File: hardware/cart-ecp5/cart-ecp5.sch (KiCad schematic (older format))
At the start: 10 parts, among them U3 FAN53541

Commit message: Remove superfluous DC-DC converter
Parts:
- removed C1: 10u, Capacitor_SMD:C_0603_1608Metric, symbol Device:C
- removed C2: 10n, Capacitor_SMD:C_0402_1005Metric, symbol Device:C
- removed C3, C4: 10u, Capacitor_SMD:C_0402_1005Metric, symbol Device:C
- removed L1: 470n, Inductor_SMD:L_0805_2012Metric, symbol Device:L
- removed R2, R3, R4: 100k, Resistor_SMD:R_0402_1005Metric, symbol Device:R
- removed R5: 267k, Resistor_SMD:R_0402_1005Metric, symbol Device:R
- removed U3: FAN53541, Package_CSP:WLCSP-20_1.934x2.434mm_Layout4x5_P0.4mm, symbol ng_pmic:FAN53541
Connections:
- net labels removed: FB1V1, GND, P1V1, P3V3, PGOOD_1V1, SW1V1
- wire segments 68 -> 0

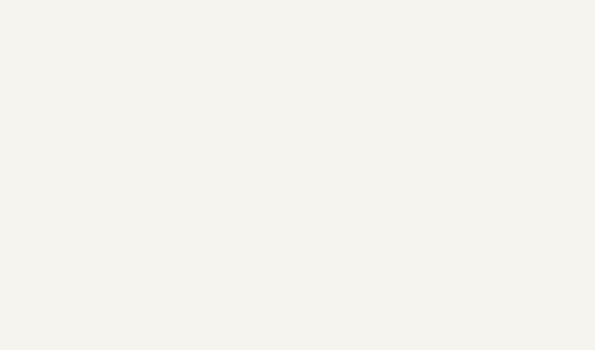
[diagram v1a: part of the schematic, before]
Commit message: Add length matching verifier script
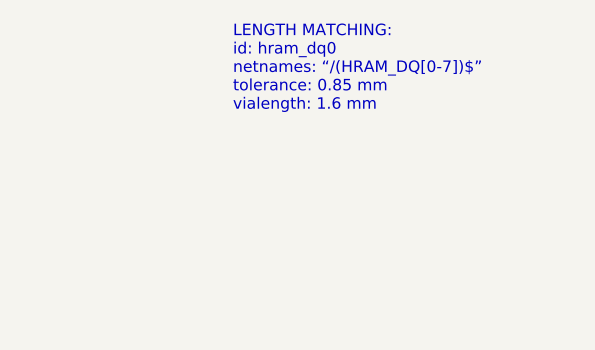
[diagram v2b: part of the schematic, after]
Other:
- note added: "LENGTH MATCHING:\nid: hram_dq0\nnetnames: “/(HRAM_DQ[0-7])$”\ntolerance: 0.85 mm\nvialength: 1.6 mm"
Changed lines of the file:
@@
 F1 "Interface-USB.sch" 50
 $EndSheet
+Text Notes 16850 1200 0    50   ~ 0
+LENGTH MATCHING:\nid: hram_dq0\nnetnames: “/(HRAM_DQ[0-7])$”\ntolerance: 0.85 mm\nvialength: 1.6 mm
 $EndSCHEMATC

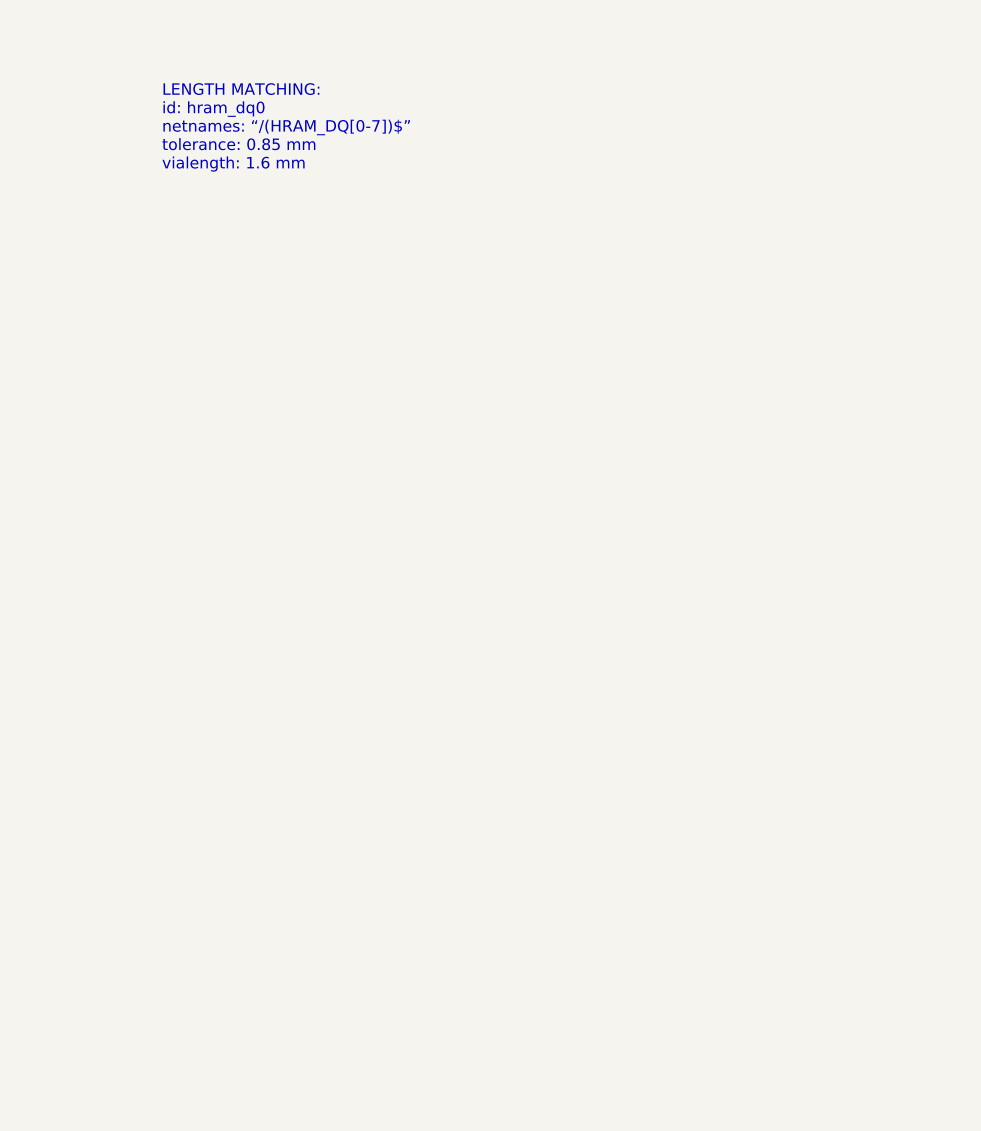
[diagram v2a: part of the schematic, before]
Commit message: Fixes to length matching script, now configured for hyperram
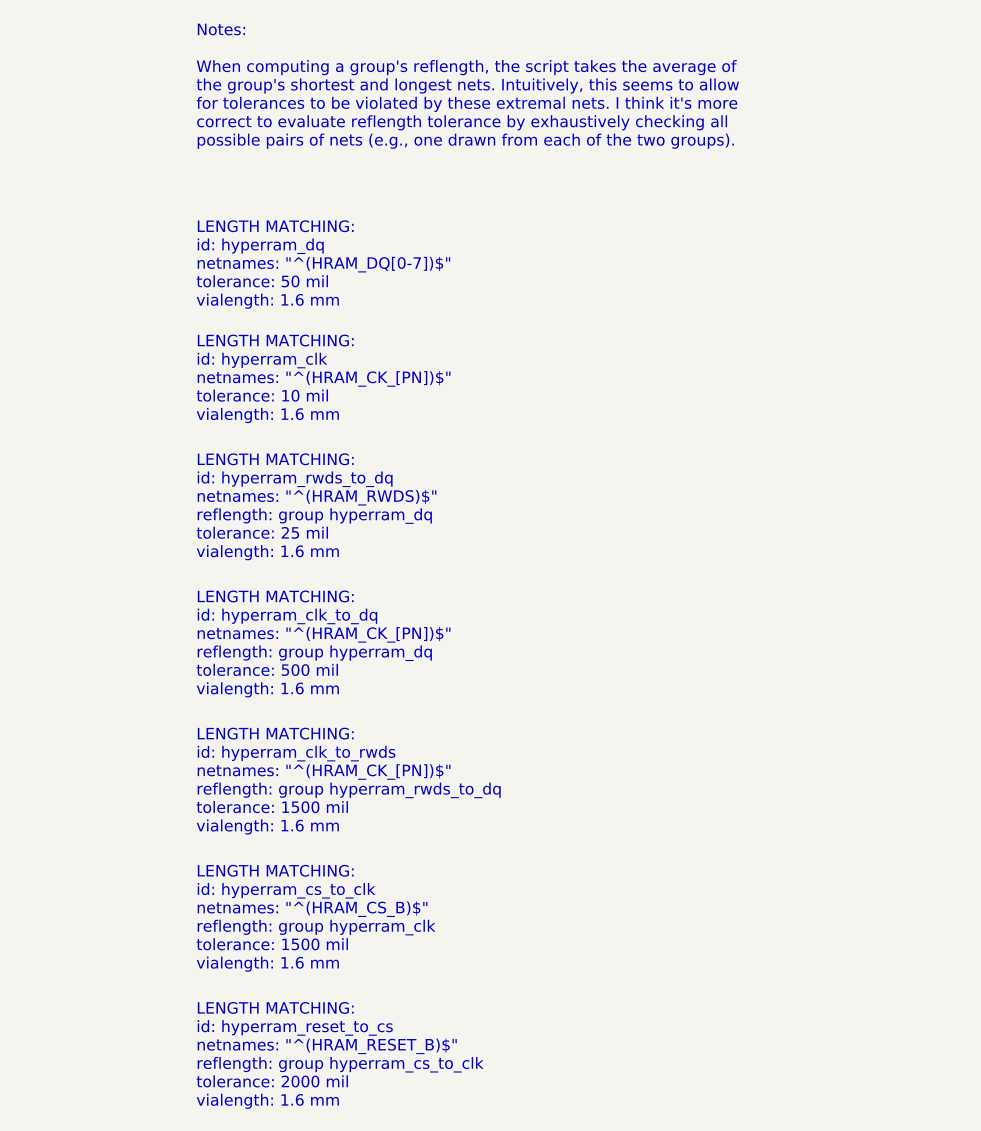
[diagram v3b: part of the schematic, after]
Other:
- note added: "LENGTH MATCHING:\nid: hyperram_clk\nnetnames: "^(HRAM_CK_[PN])$"\ntolerance: 10 mil\nvialength: 1.6 mm"
- note added: "LENGTH MATCHING:\nid: hyperram_clk_to_dq\nnetnames: "^(HRAM_CK_[PN])$"\nreflength: group hyperram_dq\ntolerance: 500 mil\nvialength: 1.6 mm"
- note added: "LENGTH MATCHING:\nid: hyperram_clk_to_rwds\nnetnames: "^(HRAM_CK_[PN])$"\nreflength: group hyperram_rwds_to_dq\ntolerance: 1500 mil\nvialength: 1.6 mm"
- note added: "LENGTH MATCHING:\nid: hyperram_cs_to_clk\nnetnames: "^(HRAM_CS_B)$"\nreflength: group hyperram_clk\ntolerance: 1500 mil\nvialength: 1.6 mm"
- note added: "LENGTH MATCHING:\nid: hyperram_dq\nnetnames: "^(HRAM_DQ[0-7])$"\ntolerance: 50 mil\nvialength: 1.6 mm"
- note added: "LENGTH MATCHING:\nid: hyperram_reset_to_cs\nnetnames: "^(HRAM_RESET_B)$"\nreflength: group hyperram_cs_to_clk\ntolerance: 2000 mil\nvialength: 1.6 mm"
- note added: "LENGTH MATCHING:\nid: hyperram_rwds_to_dq\nnetnames: "^(HRAM_RWDS)$"\nreflength: group hyperram_dq\ntolerance: 25 mil\nvialength: 1.6 mm"
- note added: "Notes:\n\nWhen computing a group's reflength, the script takes the average of\nthe group's shortest and longest nets. Intuitively, this seems to allow\nfor tolerances to be violated by these extremal nets. I think it's more\ncorrect to evaluate reflength tolerance by exhaustively checking all\npossible pairs of nets (e.g., one drawn from each of the two groups)."
- note removed: "LENGTH MATCHING:\nid: hram_dq0\nnetnames: “/(HRAM_DQ[0-7])$”\ntolerance: 0.85 mm\nvialength: 1.6 mm"
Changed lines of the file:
@@
 F1 "Interface-USB.sch" 50
 $EndSheet
-Text Notes 16850 1200 0    50   ~ 0
-LENGTH MATCHING:\nid: hram_dq0\nnetnames: “/(HRAM_DQ[0-7])$”\ntolerance: 0.85 mm\nvialength: 1.6 mm
+Text Notes 17000 1800 0    50   ~ 0
+LENGTH MATCHING:\nid: hyperram_dq\nnetnames: "^(HRAM_DQ[0-7])$"\ntolerance: 50 mil\nvialength: 1.6 mm
+Text Notes 17000 2900 0    50   ~ 0
+LENGTH MATCHING:\nid: hyperram_rwds_to_dq\nnetnames: "^(HRAM_RWDS)$"\nreflength: group hyperram_dq\ntolerance: 25 mil\nvialength: 1.6 mm
+Text Notes 17000 2300 0    50   ~ 0
+LENGTH MATCHING:\nid: hyperram_clk\nnetnames: "^(HRAM_CK_[PN])$"\ntolerance: 10 mil\nvialength: 1.6 mm
+Text Notes 17000 3500 0    50   ~ 0
+LENGTH MATCHING:\nid: hyperram_clk_to_dq\nnetnames: "^(HRAM_CK_[PN])$"\nreflength: group hyperram_dq\ntolerance: 500 mil\nvialength: 1.6 mm
+Text Notes 17000 4100 0    50   ~ 0
+LENGTH MATCHING:\nid: hyperram_clk_to_rwds\nnetnames: "^(HRAM_CK_[PN])$"\nreflength: group hyperram_rwds_to_dq\ntolerance: 1500 mil\nvialength: 1.6 mm
+Text Notes 17000 4700 0    50   ~ 0
+LENGTH MATCHING:\nid: hyperram_cs_to_clk\nnetnames: "^(HRAM_CS_B)$"\nreflength: group hyperram_clk\ntolerance: 1500 mil\nvialength: 1.6 mm
+Text Notes 17000 5300 0    50   ~ 0
+LENGTH MATCHING:\nid: hyperram_reset_to_cs\nnetnames: "^(HRAM_RESET_B)$"\nreflength: group hyperram_cs_to_clk\ntolerance: 2000 mil\nvialength: 1.6 mm
+Text Notes 17000 1100 0    50   ~ 0
+Notes:\n\nWhen computing a group's reflength, the script takes the average of\nthe group's shortest and longest nets. Intuitively, this seems to allow\nfor tolerances to be violated by these extremal nets. I think it's more\ncorrect to evaluate reflength tolerance by exhaustively checking all\npossible pairs of nets (e.g., one drawn from each of the two groups).
 $EndSCHEMATC

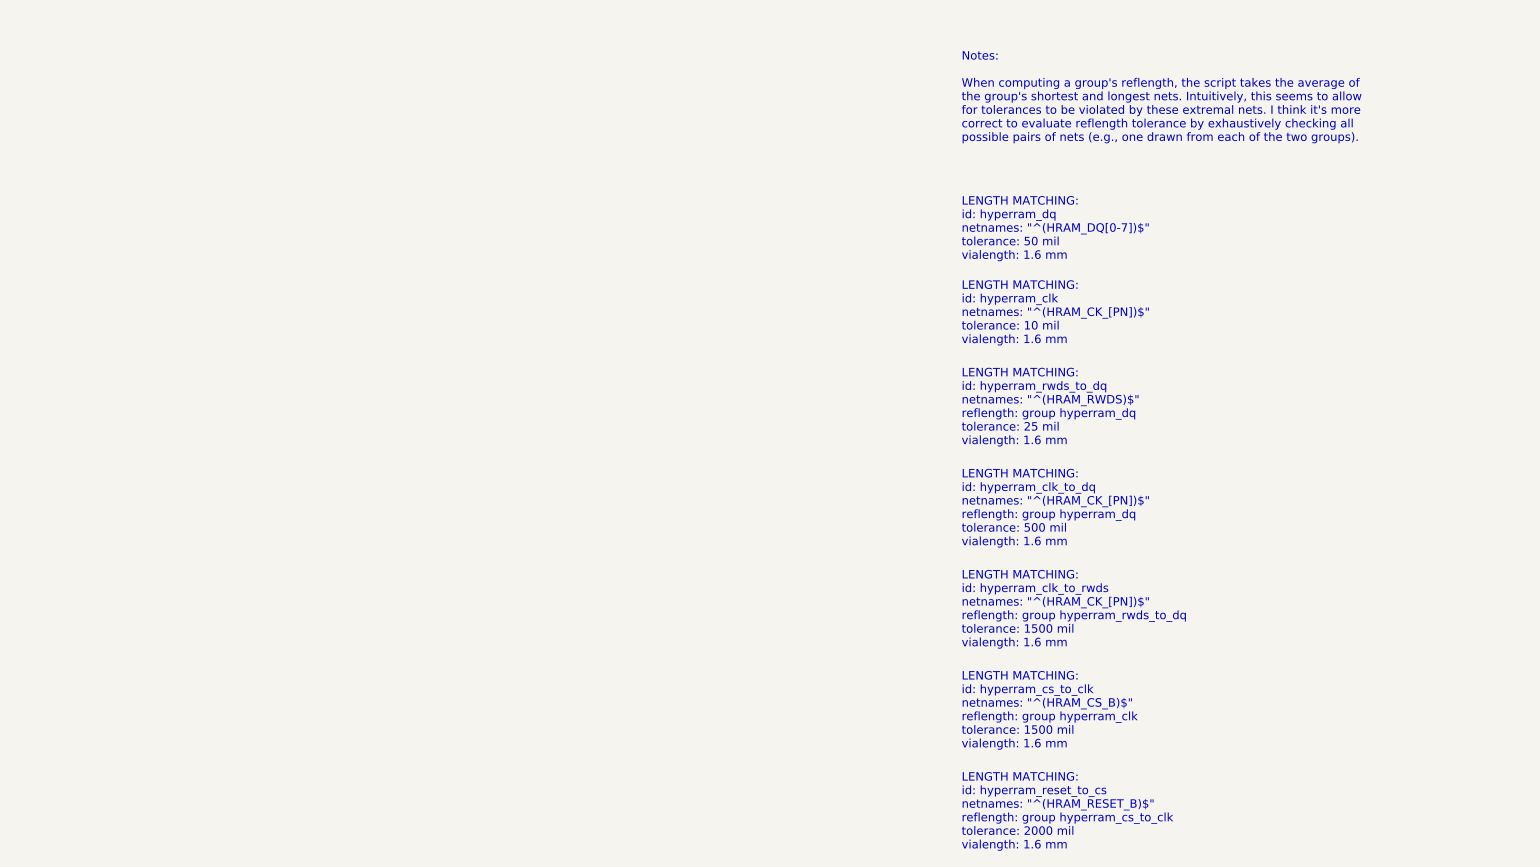
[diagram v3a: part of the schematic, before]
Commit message: Update config flash to WSON package, add HyperRAM decoupling
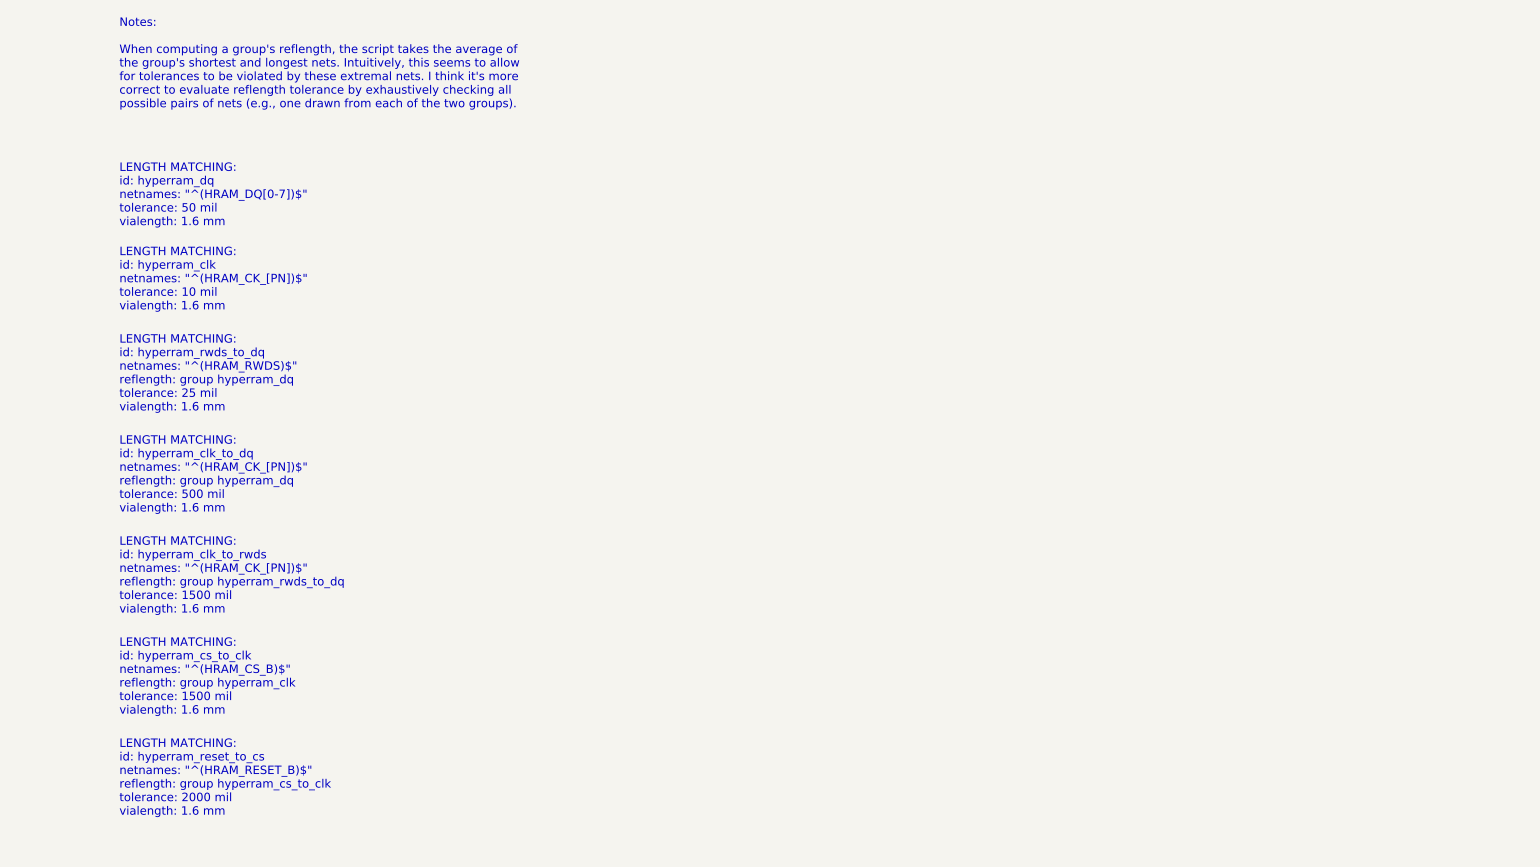
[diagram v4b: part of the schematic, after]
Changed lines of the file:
@@
 EELAYER 30 0
 EELAYER END
-$Descr A3 16535 11693
+$Descr A4 11693 8268
 encoding utf-8
 Sheet 1 7
@@
 F1 "Interface-USB.sch" 50
 $EndSheet
-Text Notes 17000 1800 0    50   ~ 0
+Text Notes 12000 1600 0    50   ~ 0
 LENGTH MATCHING:\nid: hyperram_dq\nnetnames: "^(HRAM_DQ[0-7])$"\ntolerance: 50 mil\nvialength: 1.6 mm
-Text Notes 17000 2900 0    50   ~ 0
+Text Notes 12000 2700 0    50   ~ 0
 LENGTH MATCHING:\nid: hyperram_rwds_to_dq\nnetnames: "^(HRAM_RWDS)$"\nreflength: group hyperram_dq\ntolerance: 25 mil\nvialength: 1.6 mm
-Text Notes 17000 2300 0    50   ~ 0
+Text Notes 12000 2100 0    50   ~ 0
 LENGTH MATCHING:\nid: hyperram_clk\nnetnames: "^(HRAM_CK_[PN])$"\ntolerance: 10 mil\nvialength: 1.6 mm
-Text Notes 17000 3500 0    50   ~ 0
+Text Notes 12000 3300 0    50   ~ 0
 LENGTH MATCHING:\nid: hyperram_clk_to_dq\nnetnames: "^(HRAM_CK_[PN])$"\nreflength: group hyperram_dq\ntolerance: 500 mil\nvialength: 1.6 mm
-Text Notes 17000 4100 0    50   ~ 0
+Text Notes 12000 3900 0    50   ~ 0
 LENGTH MATCHING:\nid: hyperram_clk_to_rwds\nnetnames: "^(HRAM_CK_[PN])$"\nreflength: group hyperram_rwds_to_dq\ntolerance: 1500 mil\nvialength: 1.6 mm
-Text Notes 17000 4700 0    50   ~ 0
+Text Notes 12000 4500 0    50   ~ 0
 LENGTH MATCHING:\nid: hyperram_cs_to_clk\nnetnames: "^(HRAM_CS_B)$"\nreflength: group hyperram_clk\ntolerance: 1500 mil\nvialength: 1.6 mm
-Text Notes 17000 5300 0    50   ~ 0
+Text Notes 12000 5100 0    50   ~ 0
 LENGTH MATCHING:\nid: hyperram_reset_to_cs\nnetnames: "^(HRAM_RESET_B)$"\nreflength: group hyperram_cs_to_clk\ntolerance: 2000 mil\nvialength: 1.6 mm
-Text Notes 17000 1100 0    50   ~ 0
+Text Notes 12000 900  0    50   ~ 0
 Notes:\n\nWhen computing a group's reflength, the script takes the average of\nthe group's shortest and longest nets. Intuitively, this seems to allow\nfor tolerances to be violated by these extremal nets. I think it's more\ncorrect to evaluate reflength tolerance by exhaustively checking all\npossible pairs of nets (e.g., one drawn from each of the two groups).
 $EndSCHEMATC

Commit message: Add debugging LEDs with preliminary layout
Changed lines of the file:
@@
 $Descr A4 11693 8268
 encoding utf-8
-Sheet 1 7
+Sheet 1 8
 Title ""
 Date ""
@@
 Text Notes 12000 900  0    50   ~ 0
 Notes:\n\nWhen computing a group's reflength, the script takes the average of\nthe group's shortest and longest nets. Intuitively, this seems to allow\nfor tolerances to be violated by these extremal nets. I think it's more\ncorrect to evaluate reflength tolerance by exhaustively checking all\npossible pairs of nets (e.g., one drawn from each of the two groups).
+$Sheet
+S 8000 2700 1550 950
+U 5F5BD87F
+F0 "Display" 50
+F1 "Display.sch" 50
+$EndSheet
 $EndSCHEMATC

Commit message: Add PMOD interface
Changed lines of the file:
@@
 $Descr A4 11693 8268
 encoding utf-8
-Sheet 1 8
+Sheet 1 9
 Title ""
 Date ""
@@
 $EndDescr
 $Sheet
-S 1800 2750 1750 1000
+S 1800 2700 1750 950
 U 5F4290F0
 F0 "FPGA-Power" 50
@@
 F1 "Display.sch" 50
 $EndSheet
+$Sheet
+S 3900 2700 1750 950
+U 60304B7F
+F0 "Interface-PMOD" 50
+F1 "Interface-PMOD.sch" 50
+$EndSheet
 $EndSCHEMATC
